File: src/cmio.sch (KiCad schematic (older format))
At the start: 35 parts, among them J1 USB_OTG, J2 BANK0, J3 USB_OTG, J4 DSI0, J5 CM3Lite, J6 DSI1, J7 TVOUT, J8 BANK1, J9 Micro_SD_Card_TFP09_2_12B, SW1 Reset, U1 ISL91107IR, U2 LD3985M18R, U3 LD3985M28R

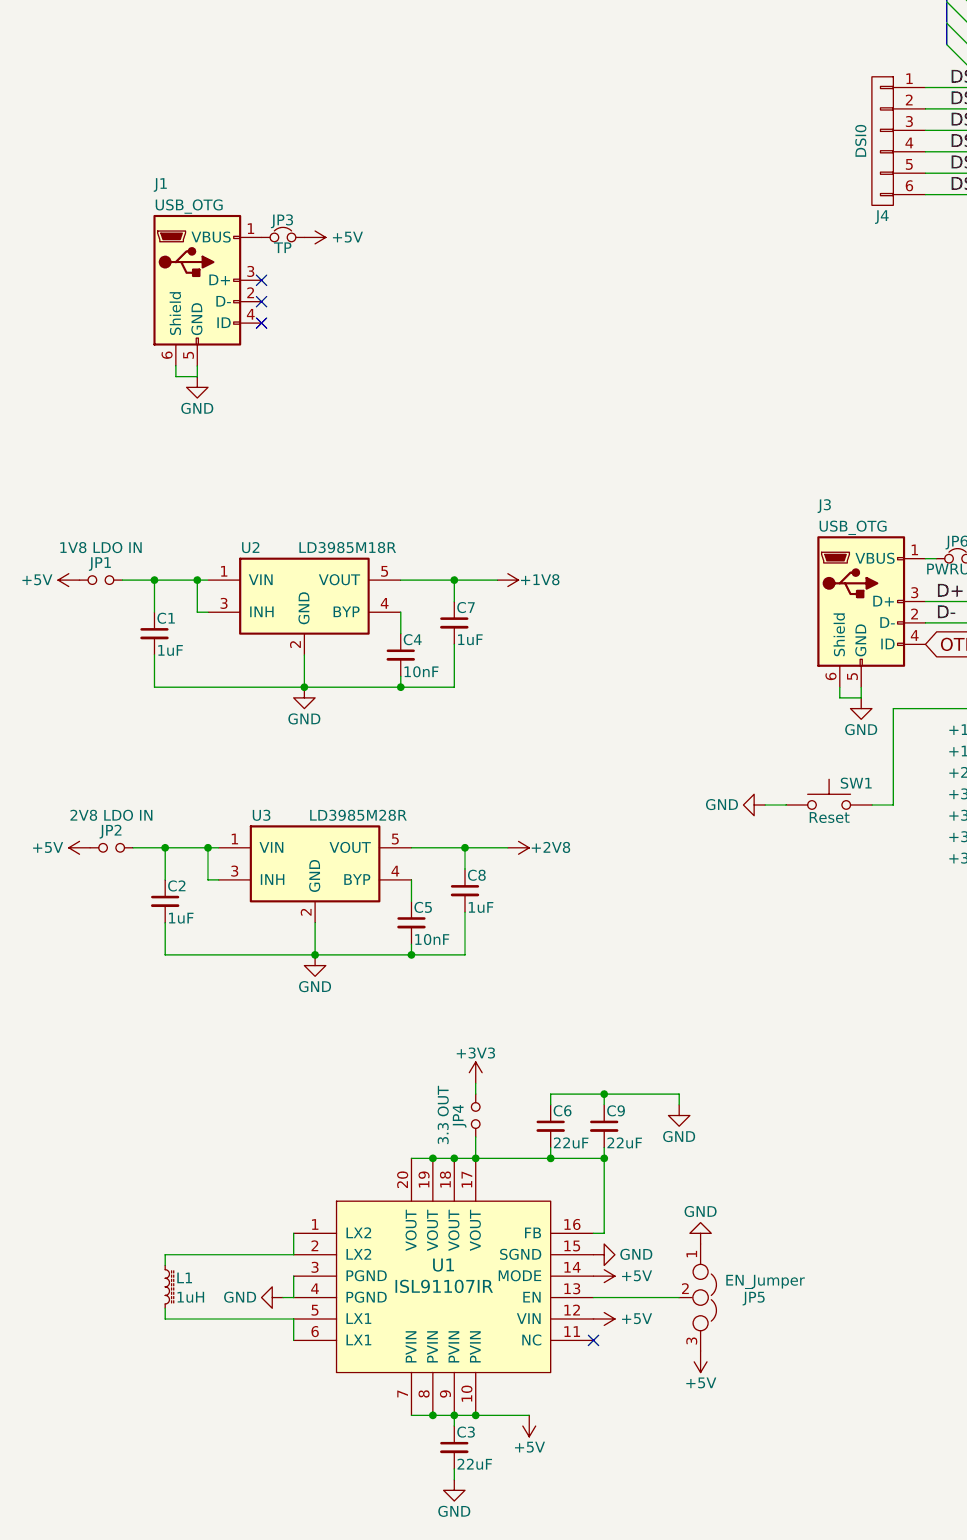
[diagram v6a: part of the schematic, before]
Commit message: Many Changes
* Add voltage test points. Fixes #10.
* Repositioned components.
* Removed some jumpers.
* Added clearer silkscreen for Reset and TV output. Fixes #8.
* Fixed Micro USB footprints. Fixes #4.

Signed-off-by: Mahyar Koshkouei <deltabeard@users.noreply.github.com>
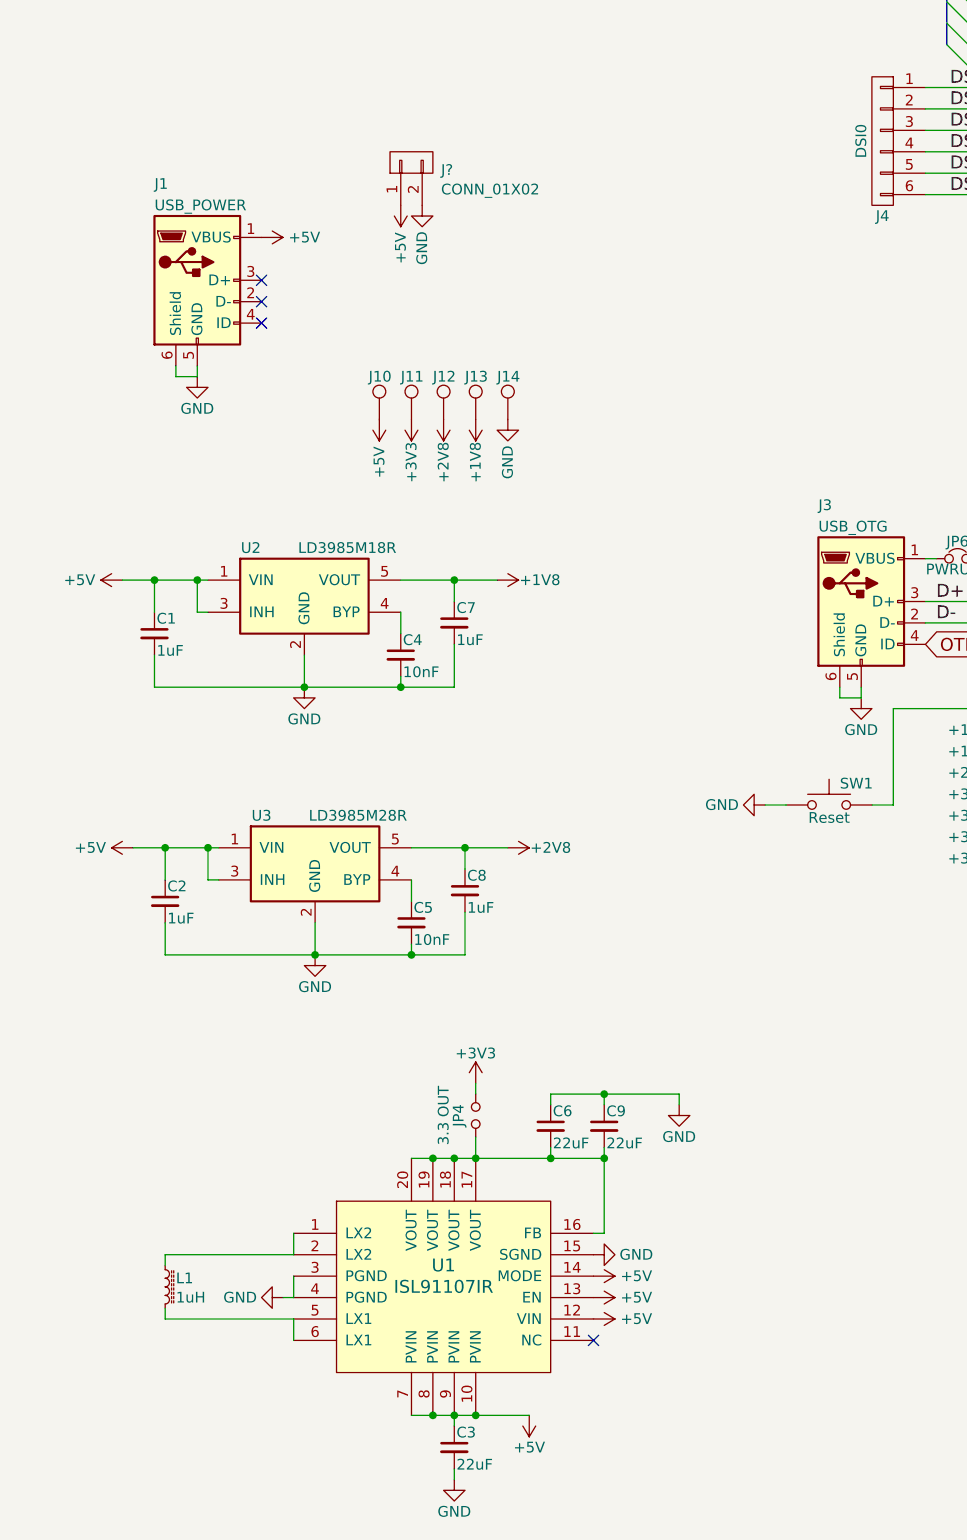
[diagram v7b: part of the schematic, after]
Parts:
- removed JP1: 1V8 LDO IN, Pin_Headers:Pin_Header_Straight_2x01_Pitch2.54mm_SMD, symbol Jumper_NO_Small
- removed JP2: 2V8 LDO IN, Pin_Headers:Pin_Header_Straight_2x01_Pitch2.54mm_SMD, symbol Jumper_NO_Small
- removed JP3: TP, Pin_Headers:Pin_Header_Straight_2x01_Pitch2.54mm_SMD, symbol Jumper_NC_Small
- removed JP5: EN_Jumper, Pin_Headers:Pin_Header_Straight_2x02_Pitch2.54mm_SMD, symbol Jumper_NC_Dual
- added J10: TEST_5V, Measurement_Points:Measurement_Point_Round-SMD-Pad_Small, symbol TEST_1P
- added J11: TEST_3V3, Measurement_Points:Measurement_Point_Round-SMD-Pad_Big, symbol TEST_1P
- added J12: TEST_2V8, Measurement_Points:Measurement_Point_Round-SMD-Pad_Big, symbol TEST_1P
- added J13: TEST_1V8, Measurement_Points:Measurement_Point_Round-SMD-Pad_Big, symbol TEST_1P
- added J14: TEST_GND, Measurement_Points:Measurement_Point_Round-SMD-Pad_Big, symbol TEST_1P
- added J?: CONN_01X02, symbol CONN_01X02
- J1: value USB_OTG -> USB_POWER
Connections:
- net +1V8: now also J13.1
- net +2V8: now also J12.1
- net +3V3: now also J11.1
- net +5V: now also C1.1, C2.1, J1.1 (VBUS), U1.13 (EN), U2.1 (VIN), U2.3 (INH), U3.1 (VIN), U3.3 (INH), J10.1, J?.1 (P1)
- net GND: now also J14.1, J?.2 (P2)

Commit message: Some changes to old design
Signed-off-by: Mahyar Koshkouei <mk@deltabeard.com>
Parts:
- removed J10: TEST_5V, Measurement_Points:Measurement_Point_Round-SMD-Pad_Small, symbol TEST_1P
- removed J13: TEST_1V8, Measurement_Points:Measurement_Point_Round-SMD-Pad_Big, symbol TEST_1P
- removed J4: DSI0, Pin_Headers:Pin_Header_Straight_2x03_Pitch2.54mm_SMD, symbol CONN_01X06
- removed J6: DSI1, Pin_Headers:Pin_Header_Straight_2x05_Pitch2.54mm_SMD, symbol CONN_01X10
- removed J?: CONN_01X02, symbol CONN_01X02
- removed JP7: Disable SD Card, Pin_Headers:Pin_Header_Straight_2x01_Pitch2.54mm_SMD, symbol Jumper_NO_Small
- added C5: 1uF, Capacitors_SMD:C_1206_HandSoldering, symbol C_Small
- J2: renamed from J11; footprint Measurement_Points:Measurement_Point_Round-SMD-Pad_Big -> Measurement_Points:Measurement_Point_Round-SMD-Pad_Small
- J3: renamed from J12; footprint Measurement_Points:Measurement_Point_Round-SMD-Pad_Big -> Measurement_Points:Measurement_Point_Round-SMD-Pad_Small
- J4: renamed from J14; footprint Measurement_Points:Measurement_Point_Round-SMD-Pad_Big -> Measurement_Points:Measurement_Point_Round-TH_Small
- renumbered C9 to C10, C10 to C11, C4 to C3, C5 to C4, C7 to C6, C3 to C7, C6 to C9, J9 to J10, J2 to J5, J3 to J6, J5 to J7, J7 to J8, J8 to J9, JP4 to JP1, JP6 to JP2, U2 to U1, U3 to U2, U1 to U3
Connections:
- net +3V3: now also C1.1, C2.1, U1.1 (VIN), U1.3 (INH), U2.1 (VIN), U2.3 (INH)
- net +5V: now also C5.1; no longer C1.1, C2.1, U1.1 (VIN), U1.3 (INH), U2.1 (VIN), U2.3 (INH)
- net GND: now also C5.2
- net DSI0_0: no longer names the net of J7.93 (DSI0_DN1)
- net DSI0_1: no longer names the net of J7.95 (DSI0_DP1)
- net DSI0_2: no longer names the net of J7.99 (DSI0_DN0)
- net DSI0_3: no longer names the net of J7.101 (DSI0_DP0)
- net DSI0_4: no longer names the net of J7.105 (DSI0_CN)
- net DSI0_5: no longer names the net of J7.107 (DSI0_CP)
- net DSI1_0: no longer names the net of J7.94 (DSI1_DP0)
- net DSI1_1: no longer names the net of J7.96 (DSI1_DN0)
- net DSI1_2: no longer names the net of J7.100 (DSI1_CP)
- net DSI1_3: no longer names the net of J7.102 (DS1_CN)
- net DSI1_4: no longer names the net of J7.106 (DSI1_DP3)
- net DSI1_5: no longer names the net of J7.108 (DSI1_DN3)
- net DSI1_6: no longer names the net of J7.112 (DSI1_DP2)
- net DSI1_7: no longer names the net of J7.114 (DSI1_DN2)
- net DSI1_8: no longer names the net of J7.118 (DSI1_DP1)
- net DSI1_9: no longer names the net of J7.120 (DSI1_DN1)
- net TVDAC: no longer names the net of J7.166 (TVDAC), J8.1 (In)
- no-connect marks 50 -> 67
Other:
- moved on the sheet: J4
